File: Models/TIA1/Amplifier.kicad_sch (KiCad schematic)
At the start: 0 parts

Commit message: Save progress
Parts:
- added C1, C2: 100 nF, 0603, symbol Device:C
- added U1: OPA828, symbol Vendor:OPA828
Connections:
- new net -15V: C2.1, U1.4 (V-)
- new net 15V: C1.1, U1.7 (V+)
- new net GND: C1.2, C2.2

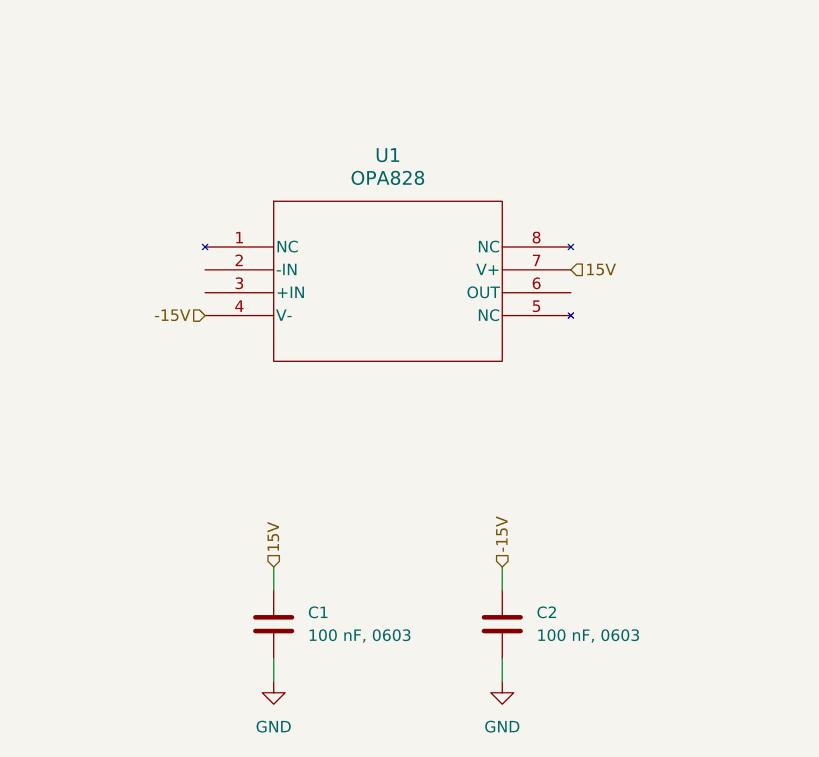
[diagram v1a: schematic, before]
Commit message: Finished with the chips for the transimpedance amplifiers
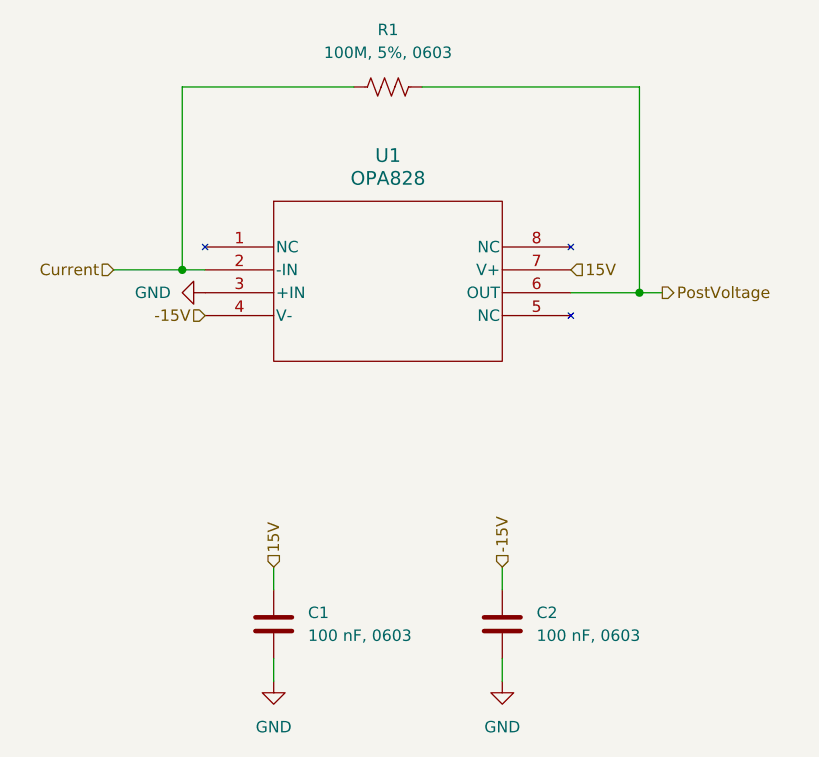
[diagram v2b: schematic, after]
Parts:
- added R1: 100M, 5%, 0603, symbol Device:R_US
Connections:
- net GND: now also U1.3 (+IN)
- net Current: now reaches U1.2 (-IN)
- net Current: now also R1.1
- net PostVoltage: now reaches U1.6 (OUT)
- net PostVoltage: now also R1.2

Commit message: Save progress
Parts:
- removed R1: 100M, 5%, 0603, symbol Device:R_US
- removed U1: OPA828, symbol Vendor:OPA828
- added R2: 100M, 5%, 0603, symbol Device:R_US
- added U2: OPA828, symbol Amplifier_Operational:OP179GS
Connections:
- net -15V: now also U2.4 (V-)
- net 15V: now also U2.7 (V+)
- net Current: now also R2.1, U2.2 (-)
- net GND: now also U2.3 (+)
- net PostVoltage: now also R2.2, U2.6

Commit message: Save progress
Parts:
- removed U2: OPA828, symbol Amplifier_Operational:OP179GS
- added U1: OPA828, symbol Amplifier_Operational:OP179GS
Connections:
- net -15V: now also U1.4 (V-)
- net 15V: now also U1.7 (V+)
- net Current: now also U1.2 (-)
- net GND: now also U1.3 (+)
- net PostVoltage: now also U1.6
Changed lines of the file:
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@@
+	)
+	(symbol
+		(lib_name "OP179GS_1")
+		(lib_id "Amplifier_Operational:OP179GS")
+		(at 116.84 76.2 0)
+		(unit 1)
+		(exclude_from_sim no)
+		(in_bom yes)
+		(on_board yes)
+		(dnp no)
+		(fields_autoplaced yes)
+		(property "Reference" "U1"
+			(at 128.27 69.7798 0)
+			(effects
+				(font
+					(size 1.27 1.27)
+				)
+			)
+		)
+		(property "Value" "OPA828"
+			(at 128.27 72.3198 0)
+			(effects
+				(font
+					(size 1.27 1.27)
+				)
+			)
+		)
+		(property "Footprint" ""
+			(at 116.84 76.2 0)
+			(effects
+				(font
+					(size 1.27 1.27)
+				)
+				(hide yes)
+			)
+		)
+		(property "Datasheet" ""
+			(at 120.65 72.39 0)
+			(effects
+				(font
+					(size 1.27 1.27)
+				)
+				(hide yes)
+			)
+		)
+		(property "Description" ""
+			(at 116.84 76.2 0)
+			(effects
+				(font
+					(size 1.27 1.27)
+				)
+				(hide yes)
+			)
+		)
+		(property "Purchase Link" ""
+			(at 116.84 76.2 0)
+			(effects
+				(font
+					(size 1.27 1.27)
+				)
+				(hide yes)
+			)
+		)
+		(pin "3"
+		)
+		(pin "2"
+		)
+		(pin "1"
+		)
+		(pin "7"
+		)
+		(pin "5"
+		)
+		(pin "4"
+		)
+		(pin "8"
+		)
+		(pin "6"
+		)
+		(instances
+			(project ""
+				(path "/f19129fc-f916-4692-924c-ee308c6b3e1d/576e9362-b988-409f-82c5-0c80cb18568a"
+					(reference "U1")
+					(unit 1)
+				)
+			)
+		)
 	)
 	(symbol
@@
 					(unit 1)
 				)
-			)
-		)
-	)
-	(symbol
-		(lib_id "Amplifier_Operational:OP179GS")
-		(at 116.84 76.2 0)
-		(unit 1)
-		(exclude_from_sim no)
-		(in_bom yes)
-		(on_board yes)
-		(dnp no)
-		(property "Reference" "U2"
-			(at 128.27 69.7798 0)
-			(effects
-				(font
-					(size 1.27 1.27)
-				)
-			)
-		)
-		(property "Value" "OPA828"
-			(at 128.27 72.3198 0)
-			(effects
-				(font
-					(size 1.27 1.27)
-				)
-			)
-		)
-		(property "Footprint" ""
-			(at 116.84 76.2 0)
-			(effects
-				(font
-					(size 1.27 1.27)
-				)
-				(hide yes)
-			)
-		)
-		(property "Datasheet" ""
-			(at 120.65 72.39 0)
-			(effects
-				(font
-					(size 1.27 1.27)
-				)
-				(hide yes)
-			)
-		)
-		(property "Description" ""
-			(at 116.84 76.2 0)
-			(effects
-				(font
-					(size 1.27 1.27)
-				)
-				(hide yes)
-			)
-		)
-		(property "Purchase Link" ""
-			(at 116.84 76.2 0)
-			(effects
-				(font
-					(size 1.27 1.27)
-				)
-				(hide yes)
-			)
-		)
-		(pin "3"
-		)
-		(pin "2"
-		)
-		(pin "1"
-		)
-		(pin "7"
-		)
-		(pin "5"
-		)
-		(pin "4"
-		)
-		(pin "8"
-		)
-		(pin "6"
-		)
-		(instances
-			(project ""
-				(path "/f19129fc-f916-4692-924c-ee308c6b3e1d/576e9362-b988-409f-82c5-0c80cb18568a"
-					(reference "U2")
-					(unit 1)
-				)
